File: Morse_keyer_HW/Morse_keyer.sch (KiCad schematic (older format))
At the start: 36 parts, among them J1 JACK_Stereo, P1 CONN_01X05, P2 CONN_01X02, SW1 SWITCH, SW2 SWITCH, SW3 SWITCH, SW4 SWITCH, SW5 SWITCH, SW6 SWITCH, U1 EFM32PG1B200F256

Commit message: Changed chip to QFN32 EFR32MG1
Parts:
- removed P1: CONN_01X05, Pin_Headers:Pin_Header_Straight_1x05_Pitch2.54mm, symbol CONN_01X05
- removed U1: EFM32PG1B200F256, Tibi lib KiCAD:QFN48, symbol EFM32PG1B200F256
- added C11: 100n, Capacitors_SMD:C_0603, symbol C_Small
- added P1: TagConnect, Connect:Tag-Connect_TC2030-IDC-NL, symbol CONN_02X03
- added U1: EFR32MG1_QFN32, Tibi lib KiCAD:QFN-32-1EP_5x5mm_Pitch0.5mm, symbol EFR32MG1_QFN32
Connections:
- net labels added: +BATT, Decouple, SWO
- net labels removed: +3.3V
- wire segments 29 -> 34
- no-connect marks 3 -> 1
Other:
- moved on the sheet: BT1, C10, C7, C8, C9, D1, P2, R13, R14

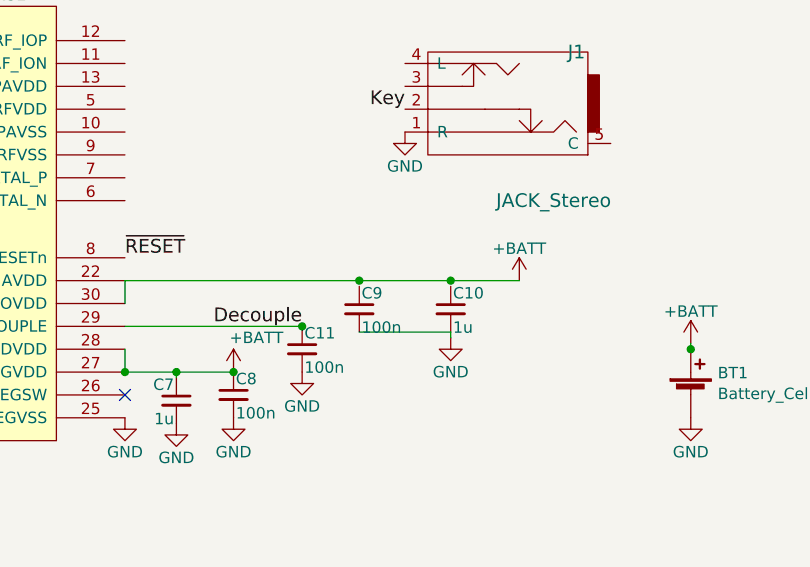
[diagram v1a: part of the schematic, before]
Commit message: Changed to QFN32 package EFR32MG1
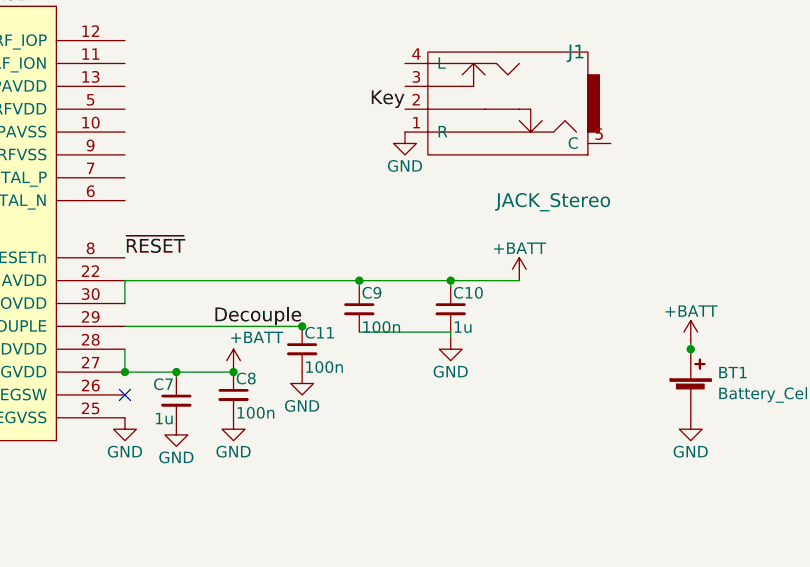
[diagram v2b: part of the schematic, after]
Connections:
- wire segments 34 -> 36
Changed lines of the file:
@@
 	0    1    1    0
 $EndComp
+Wire Wire Line
+	6575 3075 6575 3050
+Wire Wire Line
+	6175 3075 6175 3050
 $EndSCHEMATC
